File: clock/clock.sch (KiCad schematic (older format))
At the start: 166 parts, among them J1 Conn_02x05_Odd_Even, P1 Conn_WallPlug, T1 120 to 12, U1 74HC596, U10 74HC596, U11 LPC804-TSSOP24, U2 74HC596, U3 74HC596, U4 74HC596, U5 74HC596, U6 74HC596, U7 L78L33ABU, U8 74HC596, U9 74HC596

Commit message: Routing discipline broke down very early. I am going to ride this wave until it is too maddening
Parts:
- D10, D11, D12, D13, D14, D15, D16, D17, D18, D19, D20, D21, D22, D23, D24, D25, D26, D27, D28, D29, D3, D30, D31, D32, D33, D34, D35, D36, D37, D38, D39, D4, D40, D41, D42, D43, D44, D45, D46, D47, D48, D49, D5, D50, D51, D52, D53, D54, D55, D56, D57, D58, D59, D6, D60, D61, D62, D63, D64, D65, D66, D67, D68, D69, D7, D70, D71, D72, D73, D74, D8, D9: footprint LTST-S110KGKT_castellated:LTST-S110KGKT_castellated_silkV1 -> LTST-S110KGKT_castellated:LTST-S110KGKT_castellated_silkV1_rounded_rec

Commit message: Converted the 0805 to 0603. Ripped up previous routing
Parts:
- R10, R11, R12, R13, R14, R15, R16, R17, R18, R19, R20, R21, R22, R23, R24, R25, R26, R27, R28, R29, R30, R31, R32, R33, R34, R35, R36, R37, R38, R39, R4, R40, R41, R42, R43, R44, R45, R46, R47, R48, R49, R5, R50, R51, R52, R53, R54, R55, R56, R57, R58, R59, R6, R60, R61, R62, R63, R64, R65, R66, R67, R68, R69, R7, R70, R71, R72, R73, R74, R75, R8, R9: footprint Resistor_SMD:R_0805_2012Metric -> Resistor_SMD:R_0603_1608Metric

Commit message: Converted the process from LPC804 to PIC18F45K20 due to time constraints.
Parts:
- removed U11: LPC804-TSSOP24, Package_SO:TSSOP-24_4.4x7.8mm_P0.65mm, symbol MCU_NXP_LPC804:LPC804-TSSOP24
- added U11: PIC18F45K20_44-PIN_TQFP, Package_QFP:TQFP-44_10x10mm_P0.8mm, symbol MCU_PIC_18F:PIC18F45K20_44-PIN_TQFP
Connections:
- wire segments 407 -> 409
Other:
- moved on the sheet: D10, D11, D12, D13, D14, D15, D16, D17, D18, D19, D20, D21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

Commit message: Updated todo list and some tracing
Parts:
- removed J1: Conn_02x05_Odd_Even, Connector_PinHeader_1.27mm:PinHeader_2x05_P1.27mm_Vertical, symbol Connector_Generic:Conn_02x05_Odd_Even
- added C4, C5: 0.1uF, Capacitor_SMD:C_0805_2012Metric, symbol Device:C_Small
- added J1: Conn_01x06_Female, Connector_PinHeader_2.54mm:PinHeader_1x06_P2.54mm_Vertical, symbol Connector:Conn_01x06_Female
- added R1: 10K, Resistor_SMD:R_0805_2012Metric, symbol Device:R_Small_US
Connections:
- net 3v3: now also C4.1, C5.1, J1.2 (Pin_2), R1.1
- net GND: now also C4.2, C5.2, J1.3 (Pin_3)
- net Power_Clk: now reaches D2.1 (K), D75.1 (K), R3.2
- net PGM: now reaches U11.15 (KBI1/PGM/RB5)
- net PGM: now also J1.6 (Pin_6)
- net PGC: now reaches U11.16 (KBI2/PGC/RB6)
- net PGC: now also J1.5 (Pin_5)
- net PGD: now reaches U11.17 (KBI3/PGD/RB7)
- net PGD: now also J1.4 (Pin_4)
- net Vpp: now reaches U11.18 (~MCLR~/Vpp/RE3)
- net Vpp: now also J1.1 (Pin_1), R1.2
- no-connect marks 3 -> 0
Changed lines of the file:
@@
 Wire Wire Line
 	7000 1250 7100 1250
-$Comp
-L Connector_Generic:Conn_02x05_Odd_Even J1
-U 1 1 5E00183C
-P 10500 2300
-F 0 "J1" H 10550 2717 50  0000 C CNN
-F 1 "Conn_02x05_Odd_Even" H 10550 2626 50  0000 C CNN
-F 2 "Connector_PinHeader_1.27mm:PinHeader_2x05_P1.27mm_Vertical" H 10500 2300 50  0001 C CNN
-F 3 "~" H 10500 2300 50  0001 C CNN
-	1    10500 2300
-	1    0    0    -1
-$EndComp
-Text GLabel 10100 2100 0    50   Input ~ 0
-3v3
-Wire Wire Line
-	10100 2100 10300 2100
-Text GLabel 10100 2300 0    50   Input ~ 0
-GND
-Wire Wire Line
-	10300 2200 10150 2200
-Wire Wire Line
-	10150 2200 10150 2300
-Wire Wire Line
-	10150 2300 10100 2300
-Wire Wire Line
-	10300 2300 10150 2300
-Connection ~ 10150 2300
-Wire Wire Line
-	10300 2500 10150 2500
-Wire Wire Line
-	10150 2500 10150 2300
-NoConn ~ 10300 2400
-NoConn ~ 10800 2400
-NoConn ~ 10800 2300
-Text GLabel 10900 2500 2    50   Input ~ 0
-~RST
-Text GLabel 10900 2200 2    50   Input ~ 0
-SWCLK
-Text GLabel 10900 2100 2    50   Input ~ 0
-SWDIO
-Wire Wire Line
-	10800 2100 10900 2100
-Wire Wire Line
-	10800 2200 10900 2200
-Wire Wire Line
-	10800 2500 10900 2500
-Text GLabel 5950 1750 0    50   Input ~ 0
-SWDIO
-Text GLabel 5950 1650 0    50   Input ~ 0
-SWCLK
-Wire Wire Line
-	5950 1650 6300 1650
-Wire Wire Line
-	5950 1750 6300 1750
-Text GLabel 5950 1450 0    50   Input ~ 0
-~RST
-Wire Wire Line
-	5950 1450 6300 1450
 Text GLabel 7000 1350 0    50   Input ~ 0
 3v3
@@
 Wire Wire Line
 	9300 1250 9200 1250
+$Comp
+L Connector:Conn_01x06_Female J1
+U 1 1 5F0042BD
+P 10900 2050
+F 0 "J1" H 10927 2026 50  0000 L CNN
+F 1 "Conn_01x06_Female" H 10927 1935 50  0000 L CNN
+F 2 "Connector_PinHeader_2.54mm:PinHeader_1x06_P2.54mm_Vertical" H 10900 2050 50  0001 C CNN
+F 3 "~" H 10900 2050 50  0001 C CNN
+	1    10900 2050
+	1    0    0    -1
+$EndComp
+Text GLabel 10600 2050 0    50   Input ~ 0
+GND
+Wire Wire Line
+	10600 2050 10700 2050
+Text GLabel 10450 1950 0    50   Input ~ 0
+3v3
+Wire Wire Line
+	10450 1950 10550 1950
+Text GLabel 7000 2150 0    50   Input ~ 0
+PGM
+Wire Wire Line
+	7000 2150 7100 2150
+Text GLabel 7000 2250 0    50   Input ~ 0
+PGC
+Wire Wire Line
+	7000 2250 7100 2250
+Text GLabel 7000 2350 0    50   Input ~ 0
+PGD
+Wire Wire Line
+	7000 2350 7100 2350
+Text GLabel 7000 2450 0    50   Input ~ 0
+Vpp
+Wire Wire Line
+	7000 2450 7100 2450
+Text GLabel 10450 1850 0    50   Input ~ 0
+Vpp
+Wire Wire Line
+	10450 1850 10650 1850
+Text GLabel 10600 2350 0    50   Input ~ 0
+PGM
+Wire Wire Line
+	10600 2350 10700 2350
+Text GLabel 10600 2250 0    50   Input ~ 0
+PGC
+Wire Wire Line
+	10600 2250 10700 2250
+Text GLabel 10600 2150 0    50   Input ~ 0
+PGD
+Wire Wire Line
+	10600 2150 10700 2150
+$Comp
+L Device:R_Small_US R1
+U 1 1 5F3D672D
+P 10650 1600
+F 0 "R1" H 10718 1646 50  0000 L CNN
+F 1 "10K" H 10718 1555 50  0000 L CNN
+F 2 "Resistor_SMD:R_0805_2012Metric" H 10650 1600 50  0001 C CNN
+F 3 "~" H 10650 1600 50  0001 C CNN
+	1    10650 1600
+	1    0    0    -1
+$EndComp
+Wire Wire Line
+	10650 1700 10650 1850
+Connection ~ 10650 1850
+Wire Wire Line
+	10650 1850 10700 1850
+Wire Wire Line
+	10650 1500 10650 1400
+Wire Wire Line
+	10650 1400 10550 1400
+Wire Wire Line
+	10550 1400 10550 1950
+Connection ~ 10550 1950
+Wire Wire Line
+	10550 1950 10700 1950
+$Comp
+L Device:C_Small C4
+U 1 1 5F53ABE7
+P 5600 1250
+F 0 "C4" H 5692 1296 50  0000 L CNN
+F 1 "0.1uF" H 5692 1205 50  0000 L CNN
+F 2 "Capacitor_SMD:C_0805_2012Metric" H 5600 1250 50  0001 C CNN
+F 3 "~" H 5600 1250 50  0001 C CNN
+	1    5600 1250
+	1    0    0    -1
+$EndComp
+$Comp
+L Device:C_Small C5
+U 1 1 5F53B196
+P 6000 1250
+F 0 "C5" H 6092 1296 50  0000 L CNN
+F 1 "0.1uF" H 6092 1205 50  0000 L CNN
+F 2 "Capacitor_SMD:C_0805_2012Metric" H 6000 1250 50  0001 C CNN
+F 3 "~" H 6000 1250 50  0001 C CNN
+	1    6000 1250
+	1    0    0    -1
+$EndComp
+Text GLabel 5350 1350 0    50   Input ~ 0
+GND
+Text GLabel 5350 1150 0    50   Input ~ 0
+3v3
+Wire Wire Line
+	5350 1350 5600 1350
+Connection ~ 5600 1350
+Wire Wire Line
+	5600 1350 6000 1350
+Wire Wire Line
+	5350 1150 5600 1150
+Connection ~ 5600 1150
+Wire Wire Line
+	5600 1150 6000 1150
+Text GLabel 4500 1050 2    50   Input ~ 0
+Power_Clk
+Wire Wire Line
+	4200 1050 4500 1050
+Connection ~ 4200 1050
+Text GLabel 6450 1800 2    50   Input ~ 0
+Power_Clk
+Wire Wire Line
+	6150 1800 6450 1800
 $EndSCHEMATC

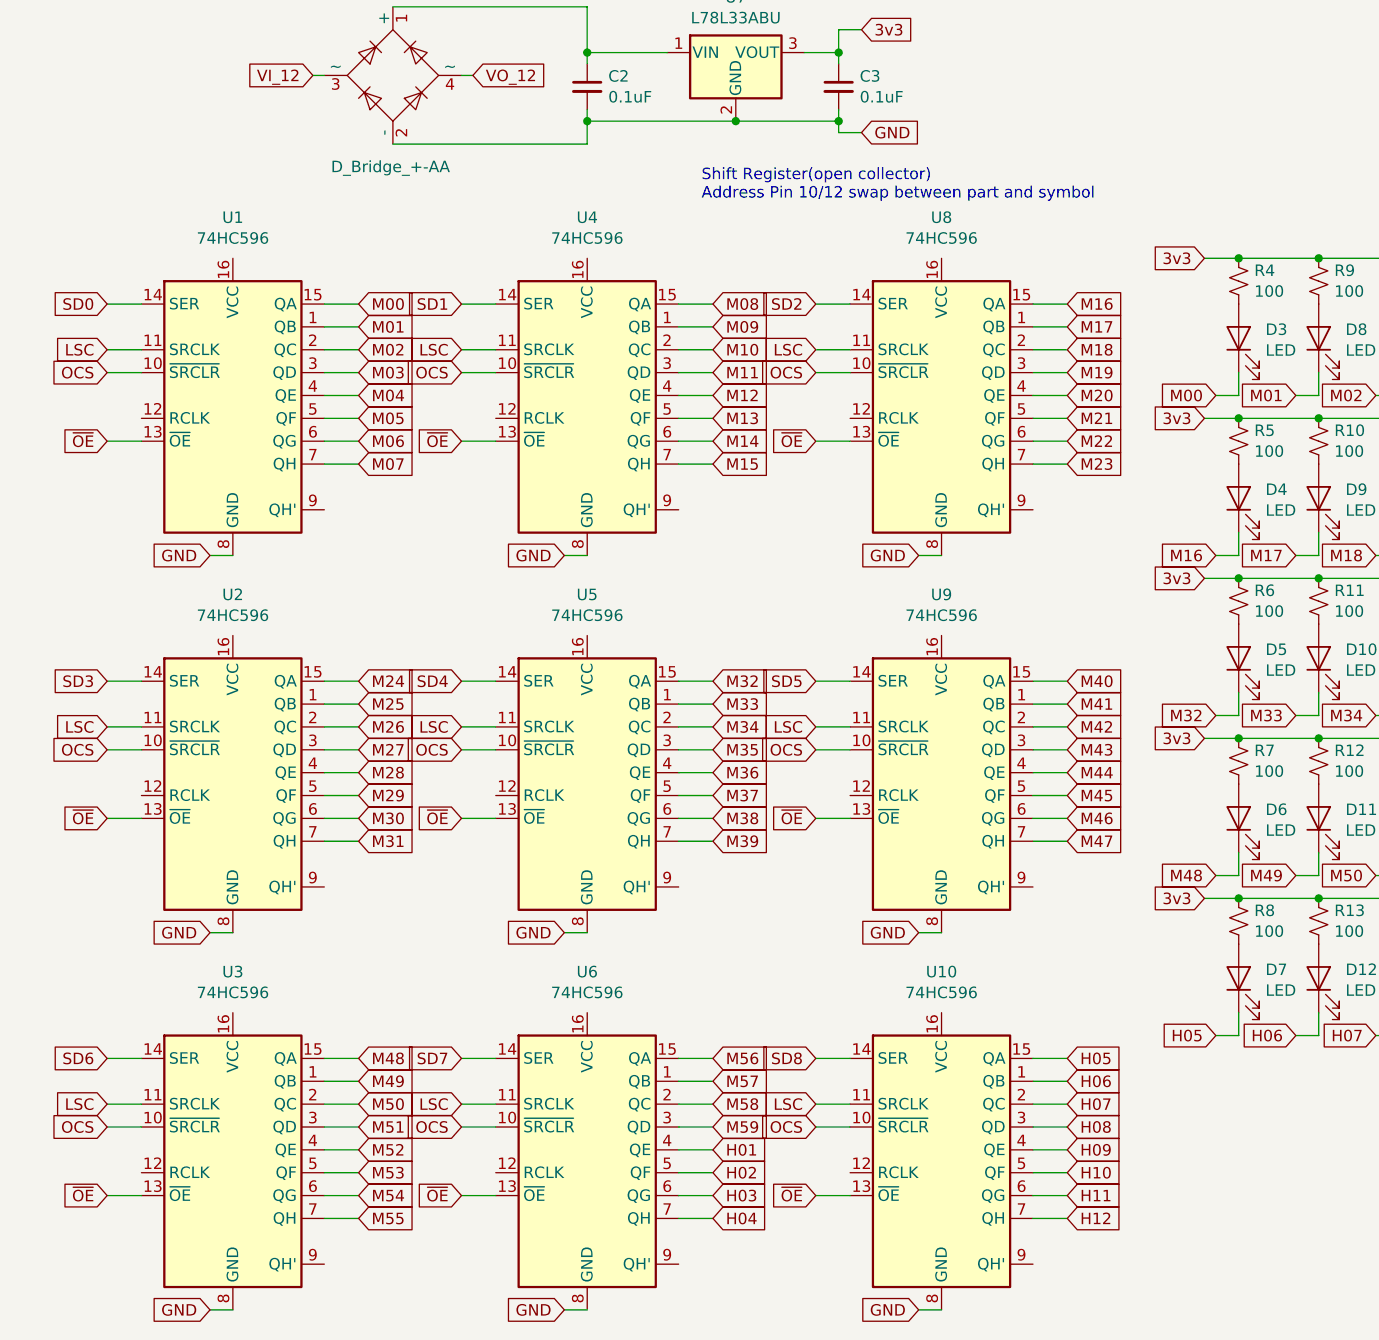
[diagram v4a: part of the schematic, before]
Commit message: Verified the part selected for shift registers. The part is way off. Updated Schematic. Updating PCB lay out.
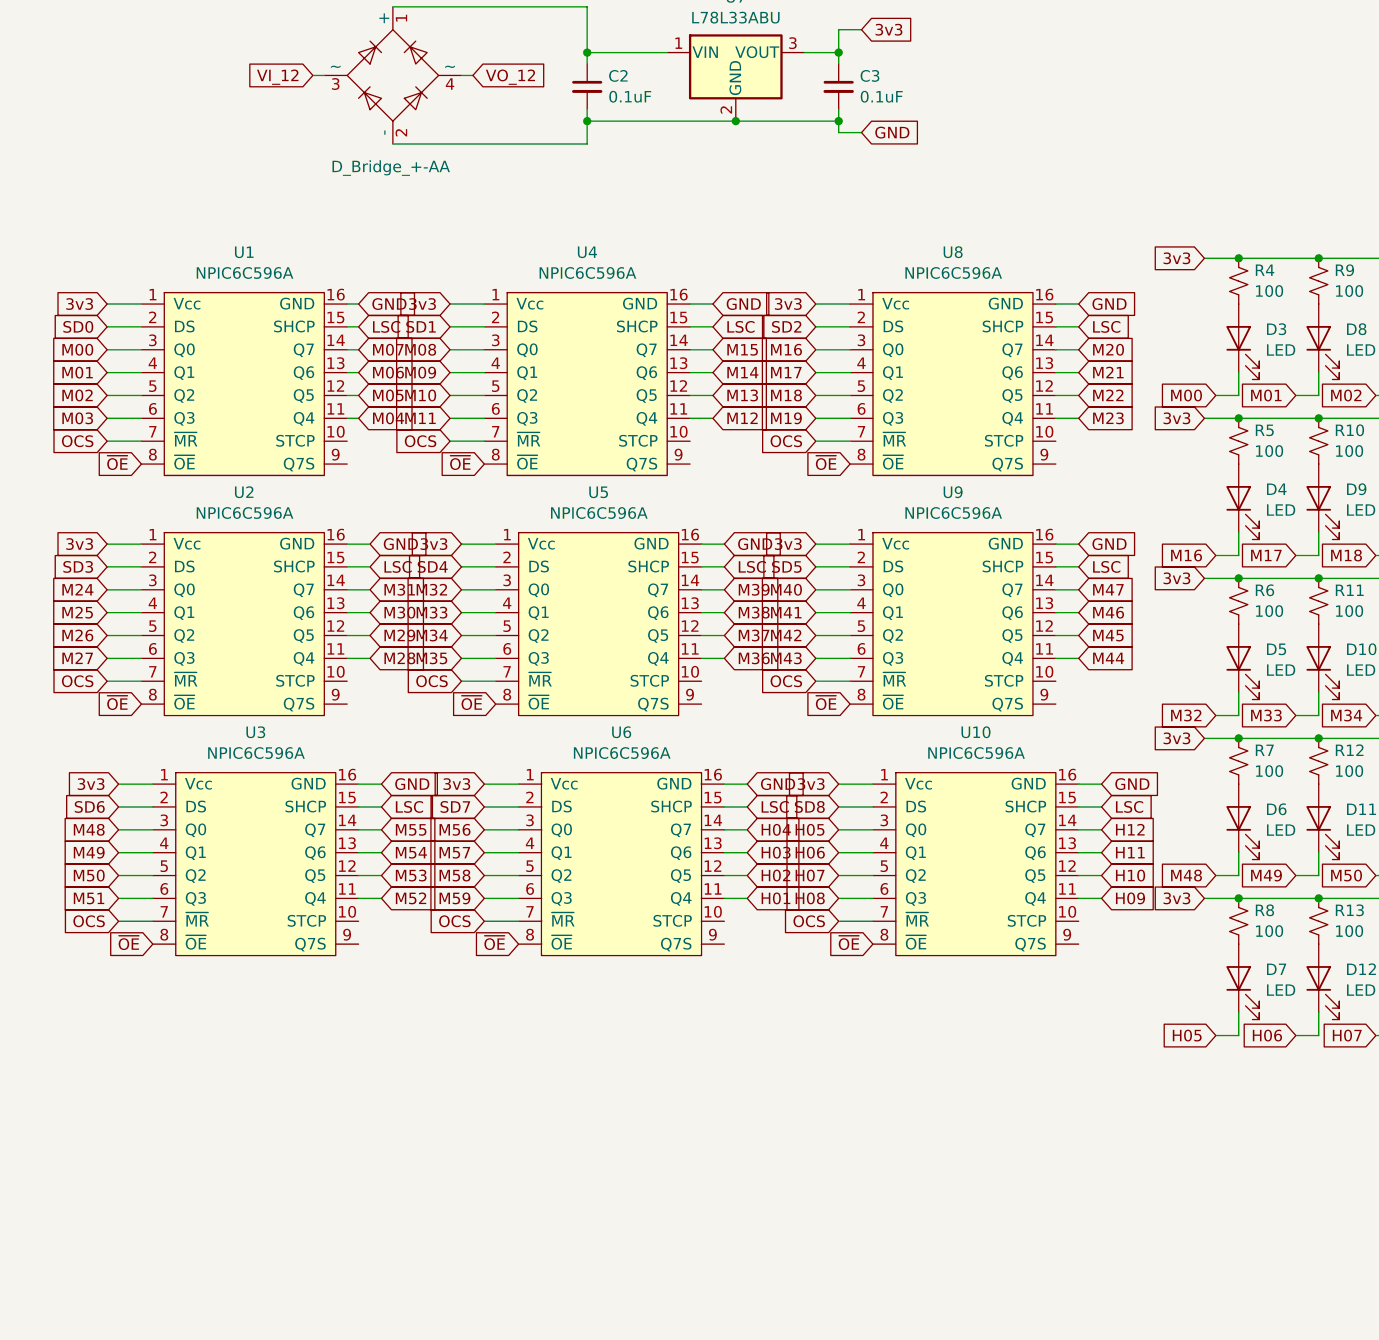
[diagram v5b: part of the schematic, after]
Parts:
- removed U1, U10, U2, U3, U4, U5, U6, U8, U9: 74HC596, Package_SO:SOP-16_4.4x10.4mm_P1.27mm, symbol 74xx:74HC596
- added U1, U10, U2, U3, U4, U5, U6, U8, U9: NPIC6C596A, Package_SO:TSSOP-16_4.4x5mm_P0.65mm, symbol Shift_reg:NPIC6C596A
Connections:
- net 3v3: now also U1.1 (Vcc), U10.1 (Vcc), U2.1 (Vcc), U3.1 (Vcc), U4.1 (Vcc), U5.1 (Vcc), U6.1 (Vcc), U8.1 (Vcc), U9.1 (Vcc)
- net GND: now also U1.16 (GND), U10.16 (GND), U2.16 (GND), U3.16 (GND), U4.16 (GND), U5.16 (GND), U6.16 (GND), U8.16 (GND), U9.16 (GND)
- net H01: now also U6.11 (Q4)
- net H02: now also U6.12 (Q5)
- net H03: now also U6.13 (Q6)
- net H04: now also U6.14 (Q7)
- net H05: now also U10.3 (Q0)
- net H06: now also U10.4 (Q1)
- net H07: now also U10.5 (Q2)
- net H08: now also U10.6 (Q3)
- net H09: now also U10.11 (Q4)
- net H10: now also U10.12 (Q5)
- net H11: now also U10.13 (Q6)
- net H12: now also U10.14 (Q7)
- net LSC: now also U1.15 (SHCP), U10.15 (SHCP), U2.15 (SHCP), U3.15 (SHCP), U4.15 (SHCP), U5.15 (SHCP), U6.15 (SHCP), U8.15 (SHCP), U9.15 (SHCP)
- net M00: now also U1.3 (Q0)
- net M01: now also U1.4 (Q1)
- net M02: now also U1.5 (Q2)
- net M03: now also U1.6 (Q3)
- net M04: now also U1.11 (Q4)
- net M05: now also U1.12 (Q5)
- net M06: now also U1.13 (Q6)
- net M07: now also U1.14 (Q7)
- net M08: now also U4.3 (Q0)
- net M09: now also U4.4 (Q1)
- net M10: now also U4.5 (Q2)
- net M11: now also U4.6 (Q3)
- net M12: now also U4.11 (Q4)
- net M13: now also U4.12 (Q5)
- net M14: now also U4.13 (Q6)
- net M15: now also U4.14 (Q7)
- net M16: now also U8.3 (Q0)
- net M17: now also U8.4 (Q1)
- net M18: now also U8.5 (Q2)
- net M19: now also U8.6 (Q3)
- net M20: now also U8.14 (Q7)
- net M21: now also U8.13 (Q6)
- net M22: now also U8.12 (Q5)
- net M23: now also U8.11 (Q4)
- net M24: now also U2.3 (Q0)
- net M25: now also U2.4 (Q1)
- net M26: now also U2.5 (Q2)
- net M27: now also U2.6 (Q3)
- net M28: now also U2.11 (Q4)
- net M29: now also U2.12 (Q5)
- net M30: now also U2.13 (Q6)
- net M31: now also U2.14 (Q7)
- net M32: now also U5.3 (Q0)
- net M33: now also U5.4 (Q1)
- net M34: now also U5.5 (Q2)
- net M35: now also U5.6 (Q3)
- net M36: now also U5.11 (Q4)
- net M37: now also U5.12 (Q5)
- net M38: now also U5.13 (Q6)
- net M39: now also U5.14 (Q7)
- net M40: now also U9.3 (Q0)
- net M41: now also U9.4 (Q1)
- net M42: now also U9.5 (Q2)
- net M43: now also U9.6 (Q3)
- net M44: now also U9.11 (Q4)
- net M45: now also U9.12 (Q5)
- net M46: now also U9.13 (Q6)
- net M47: now also U9.14 (Q7)
- net M48: now also U3.3 (Q0)
- net M49: now also U3.4 (Q1)
- net M50: now also U3.5 (Q2)
- net M51: now also U3.6 (Q3)
- net M52: now also U3.11 (Q4)
- net M53: now also U3.12 (Q5)
- net M54: now also U3.13 (Q6)
- net M55: now also U3.14 (Q7)
- net M56: now also U6.3 (Q0)
- net M57: now also U6.4 (Q1)
- net M58: now also U6.5 (Q2)
- net M59: now also U6.6 (Q3)
- net OCS: now also U1.7 (~MR), U10.7 (~MR), U2.7 (~MR), U3.7 (~MR), U4.7 (~MR), U5.7 (~MR), U6.7 (~MR), U8.7 (~MR), U9.7 (~MR)
- net SD0: now also U1.2 (DS)
- net SD1: now also U4.2 (DS)
- net SD2: now also U8.2 (DS)
- net SD3: now also U2.2 (DS)
- net SD4: now also U5.2 (DS)
- net SD5: now also U9.2 (DS)
- net SD6: now also U3.2 (DS)
- net SD7: now also U6.2 (DS)
- net SD8: now also U10.2 (DS)
- net ~OE: now also U1.8 (~OE), U10.8 (~OE), U2.8 (~OE), U3.8 (~OE), U4.8 (~OE), U5.8 (~OE), U6.8 (~OE), U8.8 (~OE), U9.8 (~OE)
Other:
- note removed: "Shift Register(open collector)\nAddress Pin 10/12 swap between part and symbol"
